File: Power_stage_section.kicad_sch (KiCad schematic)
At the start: 27 parts, among them IC1 LM66200DRLR, Q1 BSC082N10LSG, Q2 BSC082N10LSG, U2 IRS2186, U3 TLV70012_SOT23-5

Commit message: Commercial components selected
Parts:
- C12, C13, C14: footprint (none) -> Capacitor_SMD:C_0603_1608Metric_Pad1.08x0.95mm_HandSolder; Distributor Link (none) -> https://www.digikey.es/en/products/detail/murata-electronic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
- C15, C22, C23: footprint (none) -> Capacitor_SMD:C_0603_1608Metric_Pad1.08x0.95mm_HandSolder; Distributor Link (none) -> https://www.digikey.es/en/products/detail/samsung-electro-m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
- C16: footprint (none) -> Capacitor_SMD:C_0603_1608Metric_Pad1.08x0.95mm_HandSolder; Distributor Link (none) -> https://www.digikey.es/en/products/detail/yageo/CC0603KRX7R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
- C18, C19: Distributor Link (none) -> https://www.digikey.es/en/products/detail/kemet/C0603C105K4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
- C21: footprint Capacitor_SMD:CP_Elec_6.3x5.7 -> Capacitor_SMD:C_1206_3216Metric_Pad1.33x1.80mm_HandSolder; Distributor Link (none) -> https://www.digikey.es/en/products/detail/murata-electronic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
- C24: Distributor link (none) -> https://www.digikey.es/en/products/detail/samsung-electro-m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
- C25: footprint Capacitor_SMD:CP_Elec_6.3x5.7 -> Capacitor_Tantalum_SMD:CP_EIA-7260-20_AVX-M_HandSolder
- D1: footprint (none) -> LED_SMD:LED_0805_2012Metric_Pad1.15x1.40mm_HandSolder; Distributor Link (none) -> https://www.digikey.es/en/products/detail/liteon/LTST-C171K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
- IC1: footprint LM66200DRLR:SOT8 -> Package_TO_SOT_SMD:SOT-583-8; Distributor Link (none) -> https://www.digikey.es/en/products/detail/texas-instruments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
- L1: footprint (none) -> Inductor_SMD:L_12x12mm_H8mm; Distributor Link (none) -> https://www.digikey.es/en/products/detail/sumida-america-in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
- L2: footprint Inductor_SMD:L_0603_1608Metric -> Library:SC63CB; Distributor Link (none) -> https://www.digikey.es/en/products/detail/signal-transforme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
- R6: footprint Resistor_SMD:R_0603_1608Metric_Pad0.98x0.95mm_HandSolder -> Resistor_SMD:R_0805_2012Metric_Pad1.20x1.40mm_HandSolder; Distributor link (none) -> https://www.digikey.es/en/products/detail/panasonic-electro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
- R7: footprint Resistor_SMD:R_0603_1608Metric_Pad0.98x0.95mm_HandSolder -> Resistor_SMD:R_0805_2012Metric_Pad1.20x1.40mm_HandSolder; Distributor Link (none) -> https://www.digikey.es/en/products/detail/panasonic-electro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
- R9: value 800 -> 200; footprint Resistor_SMD:R_0603_1608Metric_Pad0.98x0.95mm_HandSolder -> Resistor_SMD:R_1206_3216Metric_Pad1.30x1.75mm_HandSolder; Distributor Link (none) -> https://www.digikey.es/en/products/detail/panasonic-electro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
- U2: footprint (none) -> Package_SO:SOIC-8-1EP_3.9x4.9mm_P1.27mm_EP2.29x3mm
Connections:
- net VIN is gone; now on net INPUT POWER: L2.1

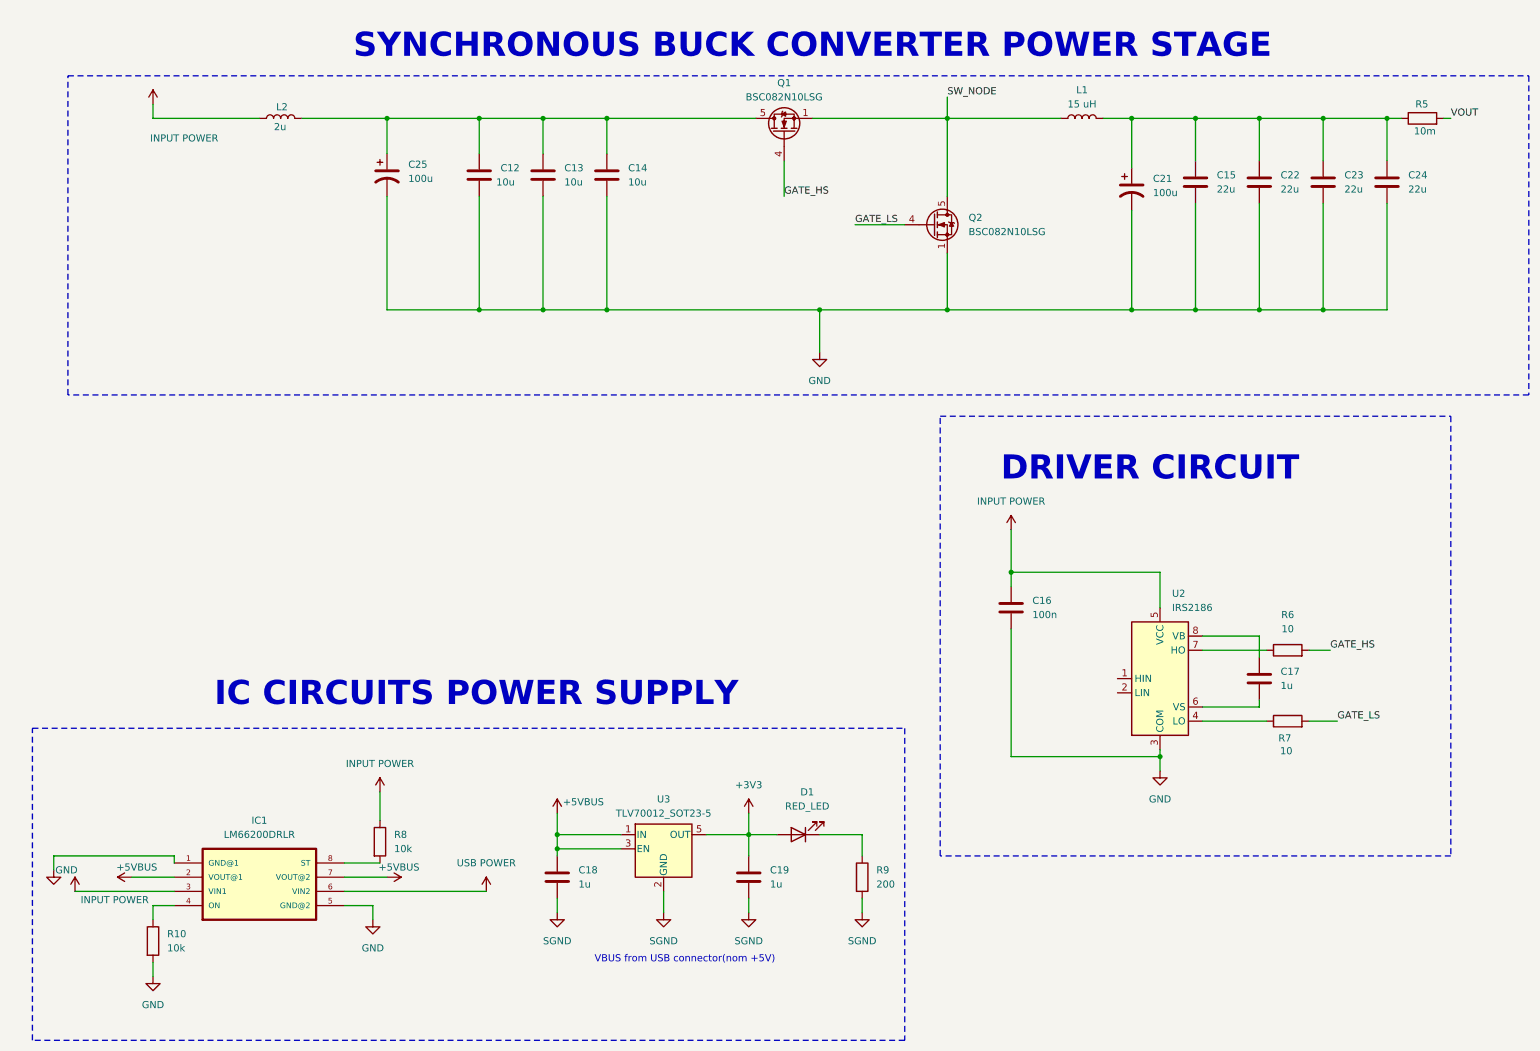
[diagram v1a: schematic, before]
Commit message: over-voltage protection added
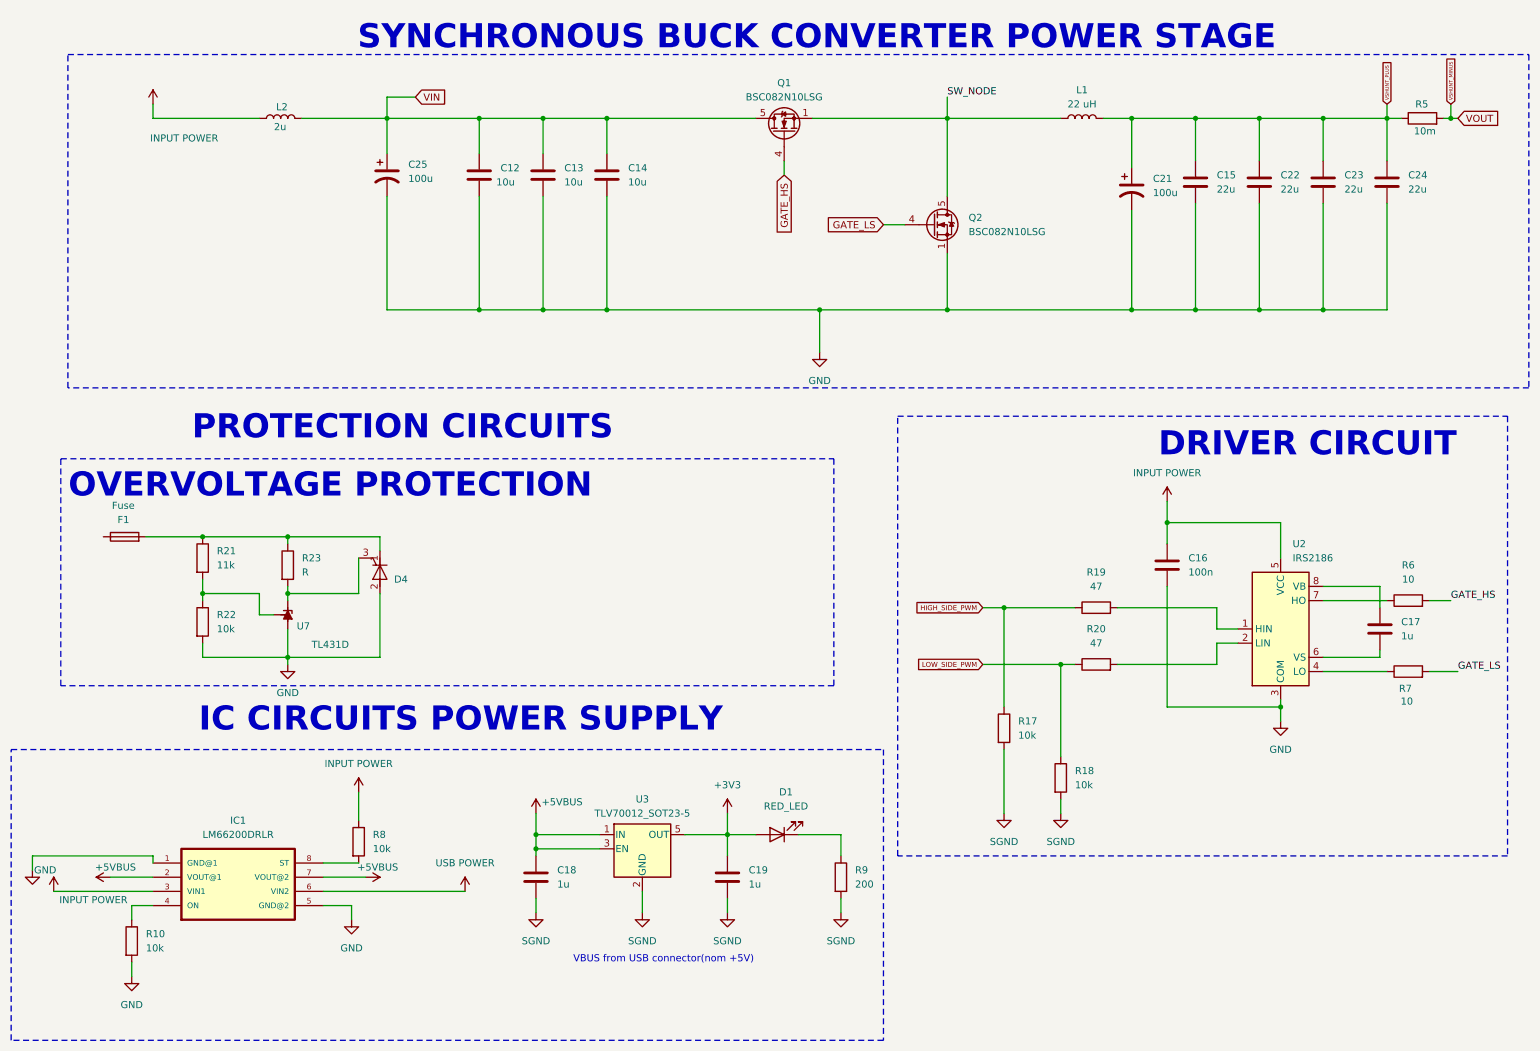
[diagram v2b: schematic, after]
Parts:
- added D4: Q_SCR_KAG, symbol Device:Q_SCR_KAG
- added F1: Fuse, symbol Device:Fuse
- added R17, R18: 10k, Resistor_SMD:R_0603_1608Metric_Pad0.98x0.95mm_HandSolder, symbol Device:R
- added R19, R20: 47, Resistor_SMD:R_0402_1005Metric_Pad0.72x0.64mm_HandSolder, symbol Device:R
- added R21: 11k, symbol Device:R
- added R22: 10k, symbol Device:R
- added R23: R, symbol Device:R
- added U7: TL431D, Package_SO:SOIC-8_3.9x4.9mm_P1.27mm, symbol Reference_Voltage:TL431D
- C17: footprint (none) -> Capacitor_SMD:C_0603_1608Metric_Pad1.08x0.95mm_HandSolder; Distributor Link (none) -> https://www.digikey.es/es/products/detail/samsung-electro-m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
- C24: footprint (none) -> Capacitor_SMD:C_0603_1608Metric_Pad1.08x0.95mm_HandSolder
- L1: value 15 uH -> 22 uH; footprint Inductor_SMD:L_12x12mm_H8mm -> Library:INDUCTOR_TDK_BUCK; Distributor Link https://www.digikey.es/en/products/detail/sumida-america-in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 -> https://www.digikey.es/es/products/detail/taiyo-yuden/NS101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
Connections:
- net GND: now also D4.2 (A), R22.2, U7.2 (A), U7.3 (A), U7.6 (A), U7.7 (A)
- net SGND: now also R17.2, R18.2
- net VSHUNT_PLUS: now reaches C15.1, C21.1, C22.1, C23.1, C24.1, L1.2, R5.1
- net VIN: now reaches C12.1, C13.1, C14.1, C25.1, L2.2, Q1.5 (D)
- net at U2.1 (HIN): now also R19.2
- net at U2.2 (LIN): now also R20.2
- new net: R21.2, R22.1, U7.8 (REF)
- new net: D4.1 (K), F1.2, R21.1, R23.1
- new net: D4.3 (G), R23.2, U7.1 (K)
- new net HIGH_SIDE_PWM: R17.1, R19.1
- new net LOW_SIDE_PWM: R18.1, R20.1
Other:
- note added: "OVERVOLTAGE PROTECTION"
- note added: "PROTECTION CIRCUITS"
- moved on the sheet: C16, C17, C18, C19, D1, IC1, R10, R6, R7, R8, R9, U2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
